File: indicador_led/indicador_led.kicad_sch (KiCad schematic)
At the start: 3 parts, among them J1 Conn_01x02_Pin

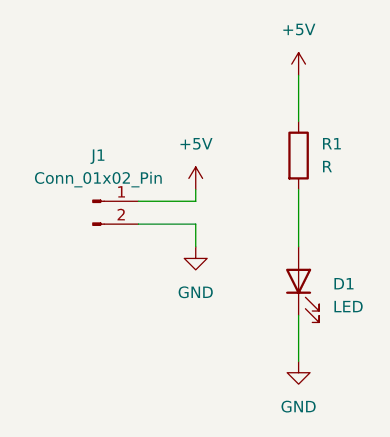
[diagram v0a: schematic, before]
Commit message: fix: altera R1 de 1k oara 680 ohmn
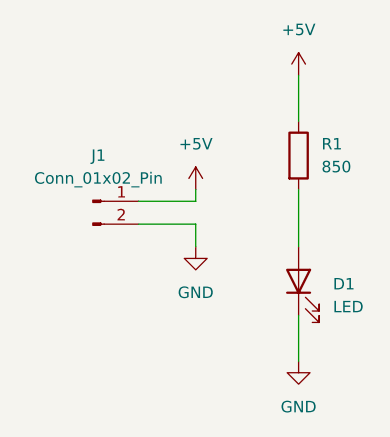
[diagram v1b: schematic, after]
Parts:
- R1: value R -> 850
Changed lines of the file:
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@@
 			)
 		)
-		(property "Value" "R"
+		(property "Value" "850"
 			(at 107.95 102.8699 0)
 			(show_name no)
